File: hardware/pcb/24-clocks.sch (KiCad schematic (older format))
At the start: 37 parts

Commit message: Change schematic to hierarchical design
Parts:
- removed BT?: BATTERY-20MM_SMD, BATTCON_20MM, symbol SparkFun-Batteries:BATTERY-20MM_SMD
- removed C? (x8): 100nF, C0603, symbol Device:C
- removed C? (x3): 22uF, symbol Device:CP
- removed J? (x2): Conn_01x04, symbol Connector_Generic:Conn_01x04
- removed J?: Conn_02x03_Odd_Even, symbol Connector_Generic:Conn_02x03_Odd_Even
- removed JP?: Jumper_NC_Small, symbol Device:Jumper_NC_Small
- removed R?: R, symbol Device:R
- removed R? (x5): 10k, R0603, symbol Device:R
- removed U?: MAX3485, symbol Interface_UART:MAX3485
- removed U?: VID66-08, TSOP-20, symbol 24-clocks:VID66-08
- removed U? (x2): VID28-05, symbol 24-clocks:VID28-05
- removed U?: AMS1117-5.0, Package_TO_SOT_SMD:SOT-223-3_TabPin2, symbol Regulator_Linear:AMS1117-5.0
- removed U?: AMS1117-3.3, Package_TO_SOT_SMD:SOT-223-3_TabPin2, symbol Regulator_Linear:AMS1117-3.3
- removed U? (x2): AH3572, Package_TO_SOT_SMD:SOT-23, symbol Sensor_Magnetic:SM351LT
- removed U?: DS1307+, Package_DIP:DIP-8_W7.62mm, symbol Timer_RTC:DS1307+
- removed U?: ESP32-WROOM-32D, RF_Module:ESP32-WROOM-32, symbol 24-clocks:ESP32-WROOM-32D
- removed U?: STM32L031K6Tx, Package_QFP:LQFP-32_7x7mm_P0.8mm, symbol MCU_ST_STM32L0:STM32L031K6Tx
- removed U?: 24LC512, symbol Memory_EEPROM:24LC512
- removed Y?: 32.768kHz, CRYSTAL-SMD-3.2X1.5MM, symbol SparkFun-Clocks:CRYSTAL-32.768KHZSMD-3.2X1.5
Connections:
- net labels removed: BOOT0, CWA, CWB, ESP-EN, ESP-IO0, ESP-RxD0, ESP-TxD0, GND, HAL-A, HAL-B, MA1, MA2, MA3, MA4, MB1, MB2, MB3, MB4, MRST, RCLK, RS485-A, RS485-B, RS485-DE, RS485-Rx, RS485-Tx, RST, STEPA, STEPB, SWDCLK, SWDIO, Serial-Rx, Serial-Tx, uC-Main-Rx, uC-Main-Tx
- wire segments 200 -> 26
- no-connect marks 1 -> 0
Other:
- moved on the sheet: R?

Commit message: Created variants
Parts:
- gave numbers to parts that had none: 2
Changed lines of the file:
@@
 EESchema Schematic File Version 4
-EELAYER 30 0
+LIBS:24-clocks-cache
+EELAYER 29 0
 EELAYER END
 $Descr A4 11693 8268
@@
 $EndDescr
 $Comp
-L power:+9V #PWR?
+L power:+9V #PWR0101
 U 1 1 5FC806BB
 P 1400 1850
-F 0 "#PWR?" H 1400 1700 50  0001 C CNN
+F 0 "#PWR0101" H 1400 1700 50  0001 C CNN
 F 1 "+9V" H 1415 2023 50  0000 C CNN
 F 2 "" H 1400 1850 50  0001 C CNN
@@
 $EndComp
 $Comp
-L power:+5V #PWR?
+L power:+5V #PWR0102
 U 1 1 5FC81029
 P 3200 1850
-F 0 "#PWR?" H 3200 1700 50  0001 C CNN
+F 0 "#PWR0102" H 3200 1700 50  0001 C CNN
 F 1 "+5V" H 3215 2023 50  0000 C CNN
 F 2 "" H 3200 1850 50  0001 C CNN
@@
 $EndComp
 $Comp
-L power:+3V3 #PWR?
+L power:+3V3 #PWR0103
 U 1 1 5FC81897
 P 3550 1850
-F 0 "#PWR?" H 3550 1700 50  0001 C CNN
+F 0 "#PWR0103" H 3550 1700 50  0001 C CNN
 F 1 "+3V3" H 3565 2023 50  0000 C CNN
 F 2 "" H 3550 1850 50  0001 C CNN
@@
 $EndComp
 $Comp
-L power:+3V3 #PWR?
+L power:+3V3 #PWR0104
 U 1 1 5FDB315A
 P 4350 4800
-F 0 "#PWR?" H 4350 4650 50  0001 C CNN
+F 0 "#PWR0104" H 4350 4650 50  0001 C CNN
 F 1 "+3V3" H 4365 4973 50  0000 C CNN
 F 2 "" H 4350 4800 50  0001 C CNN
@@
 $EndComp
 $Comp
-L Device:R R?
+L Device:R R101
 U 1 1 5FDB3160
 P 4350 5000
-F 0 "R?" H 4420 5046 50  0000 L CNN
+F 0 "R101" H 4420 5046 50  0000 L CNN
 F 1 "5k" H 4420 4955 50  0000 L CNN
 F 2 "R0603" V 4280 5000 50  0001 C CNN
@@
 	4350 4800 4350 4850
 $Comp
-L power:+3V3 #PWR?
+L power:+3V3 #PWR0105
 U 1 1 5FDB9242
 P 4650 4800
-F 0 "#PWR?" H 4650 4650 50  0001 C CNN
+F 0 "#PWR0105" H 4650 4650 50  0001 C CNN
 F 1 "+3V3" H 4665 4973 50  0000 C CNN
 F 2 "" H 4650 4800 50  0001 C CNN
@@
 $EndComp
 $Comp
-L Device:R R?
+L Device:R R102
 U 1 1 5FDB9248
 P 4650 5000
-F 0 "R?" H 4720 5046 50  0000 L CNN
+F 0 "R102" H 4720 5046 50  0000 L CNN
 F 1 "5k" H 4720 4955 50  0000 L CNN
 F 2 "R0603" V 4580 5000 50  0001 C CNN

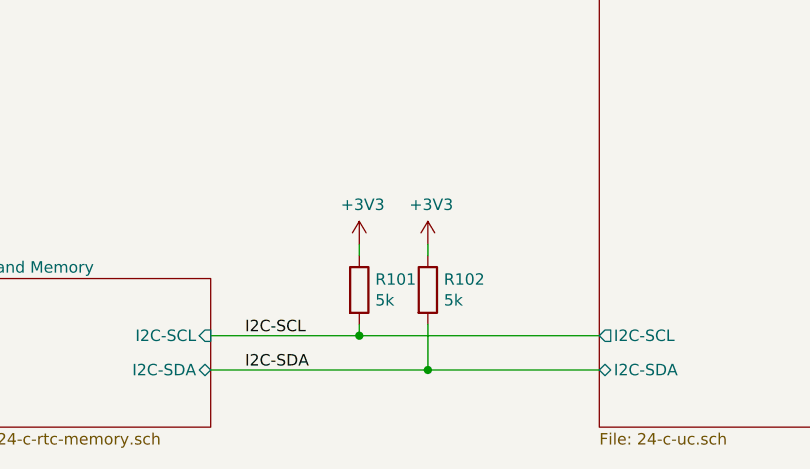
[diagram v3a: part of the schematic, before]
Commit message: Added debug connector
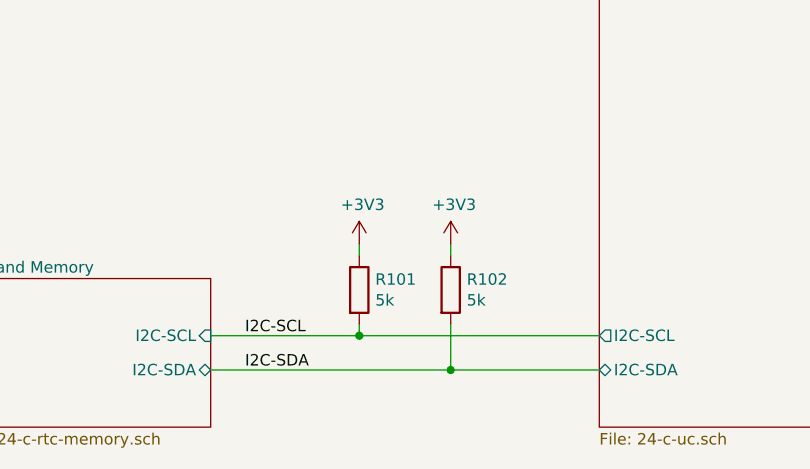
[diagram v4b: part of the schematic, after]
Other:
- moved on the sheet: R102
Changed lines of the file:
@@
 L power:+3V3 #PWR0105
 U 1 1 5FDB9242
-P 4650 4800
-F 0 "#PWR0105" H 4650 4650 50  0001 C CNN
-F 1 "+3V3" H 4665 4973 50  0000 C CNN
-F 2 "" H 4650 4800 50  0001 C CNN
-F 3 "" H 4650 4800 50  0001 C CNN
-	1    4650 4800
+P 4750 4800
+F 0 "#PWR0105" H 4750 4650 50  0001 C CNN
+F 1 "+3V3" H 4765 4973 50  0000 C CNN
+F 2 "" H 4750 4800 50  0001 C CNN
+F 3 "" H 4750 4800 50  0001 C CNN
+	1    4750 4800
 	1    0    0    -1
 $EndComp
@@
 L Device:R R102
 U 1 1 5FDB9248
-P 4650 5000
-F 0 "R102" H 4720 5046 50  0000 L CNN
-F 1 "5k" H 4720 4955 50  0000 L CNN
-F 2 "R0603" V 4580 5000 50  0001 C CNN
-F 3 "~" H 4650 5000 50  0001 C CNN
-	1    4650 5000
+P 4750 5000
+F 0 "R102" H 4820 5046 50  0000 L CNN
+F 1 "5k" H 4820 4955 50  0000 L CNN
+F 2 "R0603" V 4680 5000 50  0001 C CNN
+F 3 "~" H 4750 5000 50  0001 C CNN
+	1    4750 5000
 	1    0    0    -1
 $EndComp
 Wire Wire Line
-	4650 4800 4650 4850
+	4750 4800 4750 4850
 Wire Wire Line
 	4350 5150 4350 5200
@@
 	7150 5350 8300 5350
 Wire Wire Line
-	4650 5150 4650 5350
-Connection ~ 4650 5350
-Wire Wire Line
-	3700 5350 4650 5350
+	4750 5150 4750 5350
 Wire Wire Line
 	3700 5200 4350 5200
 Wire Wire Line
 	4350 5200 5400 5200
+Connection ~ 4750 5350
 Wire Wire Line
-	4650 5350 5400 5350
+	4750 5350 5400 5350
+Wire Wire Line
+	3700 5350 4750 5350
 $EndSCHEMATC
